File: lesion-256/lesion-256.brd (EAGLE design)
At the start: 32 x 32 mm, 9 parts

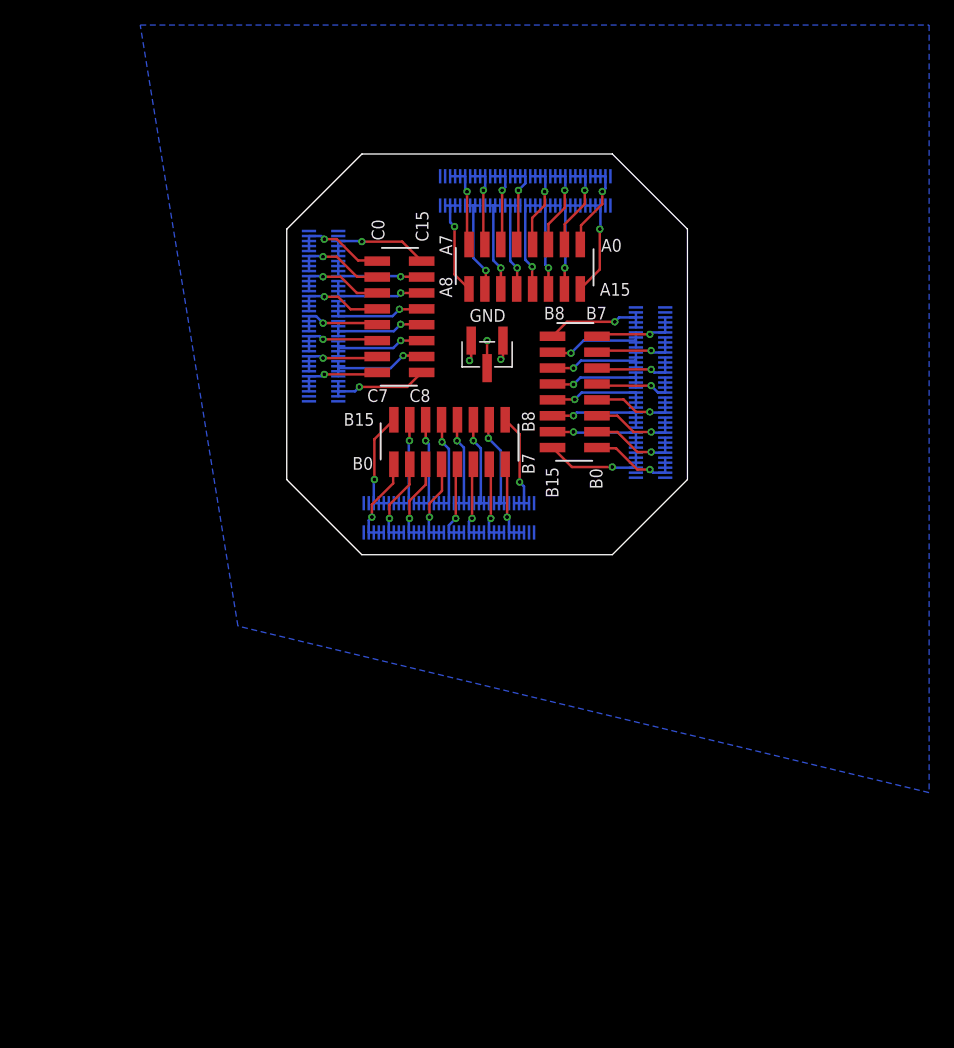
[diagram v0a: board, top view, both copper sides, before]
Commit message: Added another breakout for electrolesioning with eib-64
- I just put it as breakaway board on the existing lesion-256 board
- I will change the name of this directory and all files after this
commit
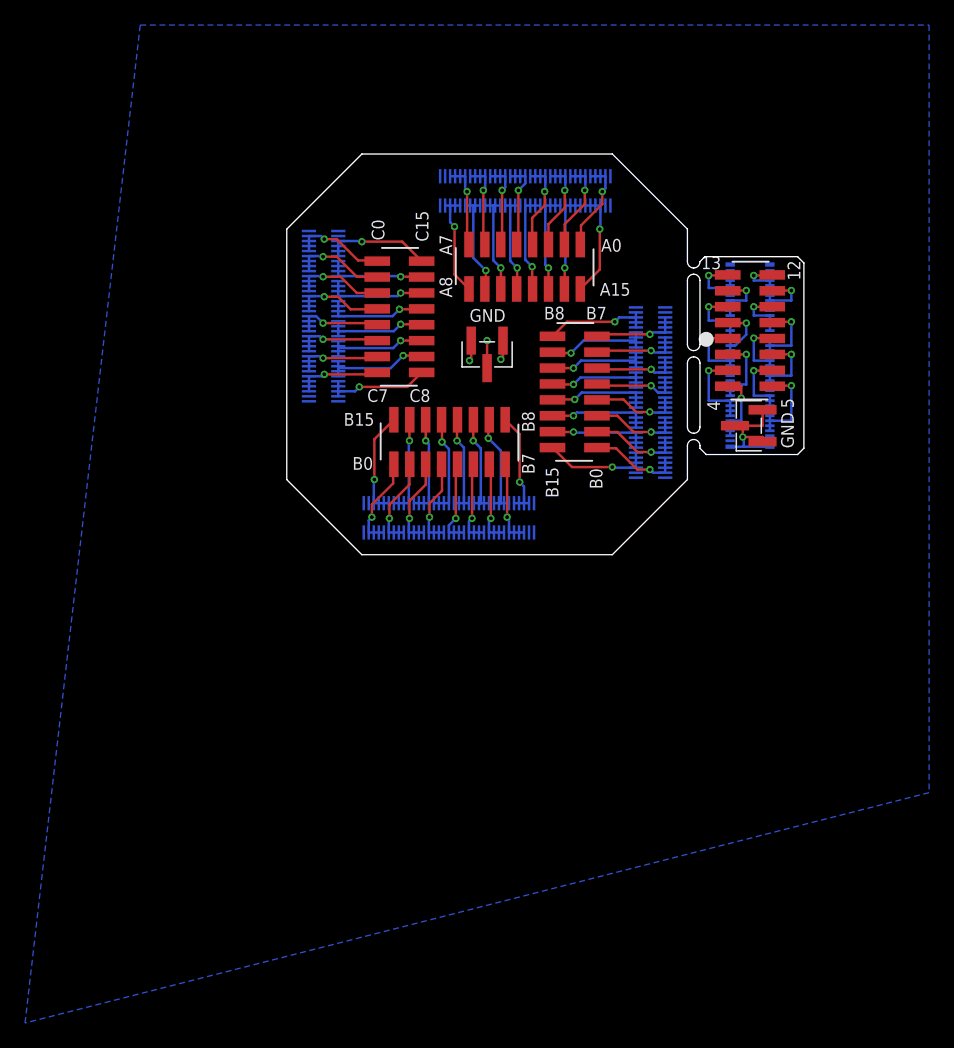
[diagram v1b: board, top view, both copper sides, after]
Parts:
- added J1: DF40C-70DP-0.4V(51), jonnew:DF40-70HEAD-LESS-SILK
- added J4: (no value), jonnew:JP2X8_SMD_0.5"
- added J7: (no value), jonnew:JP3_SMD-0.05
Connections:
- new net N$1: J1.53, J1.54, J1.55, J1.56, J4.12
- new net N$10: J1.26, J1.27, J1.28, J1.29, J4.2
- new net N$11: J1.30, J1.31, J1.32, J1.33, J4.1
- new net N$12: J1.37, J1.38, J1.39, J1.40, J4.16
- new net N$13: J1.41, J1.42, J1.43, J1.44, J4.15
- new net N$14: J1.45, J1.46, J1.47, J1.48, J4.14
- new net N$15: J1.49, J1.50, J1.51, J1.52, J4.13
- new net N$2: J1.57, J1.58, J1.59, J1.60, J4.11
- new net N$3: J1.61, J1.62, J1.63, J1.64, J4.10
- new net N$32: J1.6, J1.7, J1.8, J1.9, J4.7
- new net N$4: J1.2, J1.3, J1.4, J1.5, J4.8
- new net N$5: J1.65, J1.66, J1.67, J1.68, J4.9
- new net N$6: J1.10, J1.11, J1.12, J1.13, J4.6
- new net N$7: J1.14, J1.15, J1.16, J1.17, J4.5
- new net N$8: J1.18, J1.19, J1.20, J1.21, J4.4
- new net N$9: J1.22, J1.23, J1.24, J1.25, J4.3
- net AGND: now also J1.1, J1.69, J1.M1, J1.M2, J1.M3, J1.M4, J7.1, J7.2, J7.3
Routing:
- net AGND: track 5.42 -> 15.8 mm, vias 3 -> 4
- net N$11: track 0.00 -> 7.29 mm, vias 0 -> 1
- net N$13: track 0.00 -> 6.87 mm, vias 0 -> 1
- net N$10: track 0.00 -> 6.71 mm, vias 0 -> 1
- net N$7: track 0.00 -> 6.41 mm, vias 0 -> 1
- net N$14: track 0.00 -> 6.36 mm, vias 0 -> 1
- net N$15: track 0.00 -> 6.28 mm, vias 0 -> 1
- net N$9: track 0.00 -> 6.15 mm, vias 0 -> 1
- net N$12: track 0.00 -> 5.92 mm, vias 0 -> 1
- net N$8: track 0.00 -> 5.79 mm, vias 0 -> 1
- net N$2: track 0.00 -> 5.55 mm, vias 0 -> 1
- net N$5: track 0.00 -> 5.49 mm, vias 0 -> 1
- net N$1: track 0.00 -> 5.28 mm, vias 0 -> 1
- net N$32: track 0.00 -> 5.27 mm, vias 0 -> 1
- net N$3: track 0.00 -> 4.78 mm, vias 0 -> 1
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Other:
- board size 32 x 32 mm -> 41.3 x 32 mm
- board text added: "12"
- board text added: "13"
- board text added: "4"
- board text added: "5"
- board text added: "LESION-64-128-256"
- board text removed: "LESION-256"
